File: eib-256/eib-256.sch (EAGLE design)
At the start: 36 parts

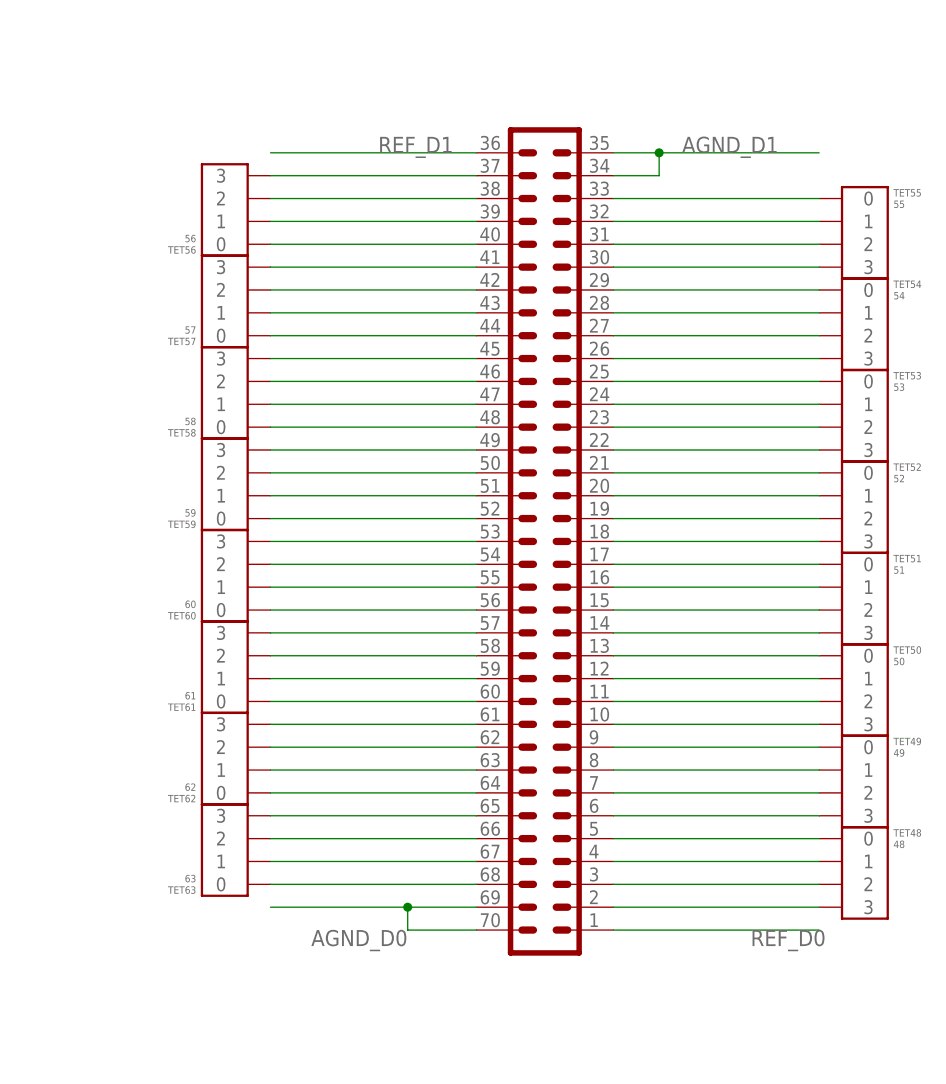
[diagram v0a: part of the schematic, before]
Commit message: More than half way through 256 channel eib layout.
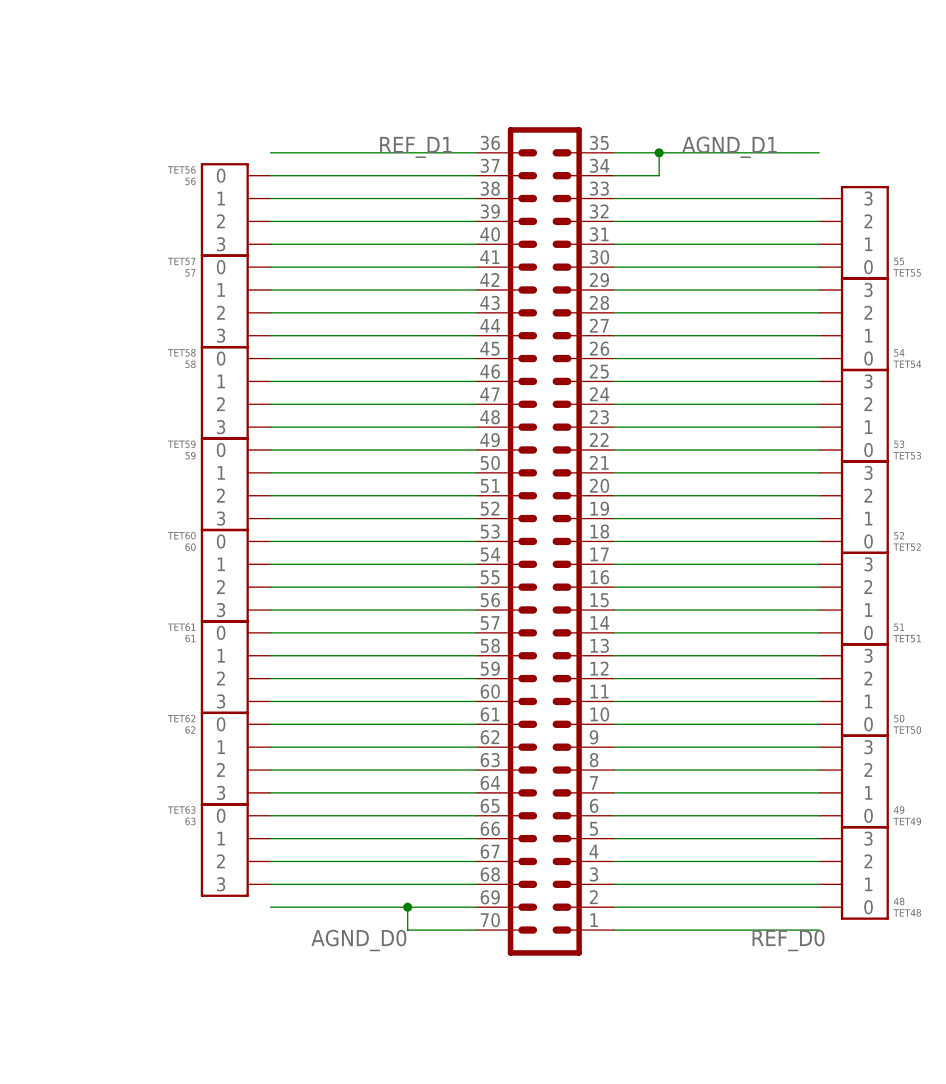
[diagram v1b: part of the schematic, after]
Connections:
- net N$1: now also D.2, TET48.0; no longer D.33, TET55.0
- net N$10: now also D.11, TET50.1; no longer D.24, TET53.1
- net N$11: now also D.12, TET50.2; no longer D.23, TET53.2
- net N$12: now also D.13, TET50.3; no longer D.22, TET53.3
- net N$13: now also D.14, TET51.0; no longer D.21, TET52.0
- net N$14: now also D.15, TET51.1; no longer D.20, TET52.1
- net N$15: now also D.16, TET51.2; no longer D.19, TET52.2
- net N$16: now also D.17, TET51.3; no longer D.18, TET52.3
- net N$17: now also D.18, TET52.0; no longer D.17, TET51.0
- net N$18: now also D.19, TET52.1; no longer D.16, TET51.1
- net N$19: now also D.20, TET52.2; no longer D.15, TET51.2
- net N$2: now also D.3, TET48.1; no longer D.32, TET55.1
- net N$20: now also D.21, TET52.3; no longer D.14, TET51.3
- net N$21: now also D.22, TET53.0; no longer D.13, TET50.0
- net N$22: now also D.23, TET53.1; no longer D.12, TET50.1
- net N$23: now also D.24, TET53.2; no longer D.11, TET50.2
- net N$24: now also D.25, TET53.3; no longer D.10, TET50.3
- net N$25: now also D.26, TET54.0; no longer D.9, TET49.0
- net N$26: now also D.27, TET54.1; no longer D.8, TET49.1
- net N$27: now also D.28, TET54.2; no longer D.7, TET49.2
- net N$28: now also D.29, TET54.3; no longer D.6, TET49.3
- net N$29: now also D.30, TET55.0; no longer D.5, TET48.0
- net N$3: now also D.4, TET48.2; no longer D.31, TET55.2
- net N$30: now also D.31, TET55.1; no longer D.4, TET48.1
- net N$31: now also D.32, TET55.2; no longer D.3, TET48.2
- net N$32: now also D.42, TET57.1; no longer D.38, TET56.2
- net N$33: now also D.43, TET57.2; no longer D.39, TET56.1
- net N$34: now also D.44, TET57.3; no longer D.40, TET56.0
- net N$35: now also D.45, TET58.0; no longer D.41, TET57.3
- net N$36: now also D.46, TET58.1; no longer D.42, TET57.2
- net N$37: now also D.47, TET58.2; no longer D.43, TET57.1
- net N$38: now also D.48, TET58.3; no longer D.44, TET57.0
- net N$39: now also D.49, TET59.0; no longer D.45, TET58.3
- net N$4: now also D.5, TET48.3; no longer D.30, TET55.3
- net N$40: now also D.50, TET59.1; no longer D.46, TET58.2
- net N$41: now also D.51, TET59.2; no longer D.47, TET58.1
- net N$42: now also D.52, TET59.3; no longer D.48, TET58.0
- net N$43: now also D.53, TET60.0; no longer D.49, TET59.3
- net N$44: now also D.54, TET60.1; no longer D.50, TET59.2
- net N$45: now also D.55, TET60.2; no longer D.51, TET59.1
- net N$46: now also D.56, TET60.3; no longer D.52, TET59.0
- net N$47: now also D.57, TET61.0; no longer D.53, TET60.3
- net N$48: now also D.58, TET61.1; no longer D.54, TET60.2
- net N$49: now also D.59, TET61.2; no longer D.55, TET60.1
- net N$5: now also D.6, TET49.0; no longer D.29, TET54.0
- net N$50: now also D.60, TET61.3; no longer D.56, TET60.0
- net N$51: now also D.61, TET62.0; no longer D.57, TET61.3
- net N$52: now also D.62, TET62.1; no longer D.58, TET61.2
- net N$53: now also D.63, TET62.2; no longer D.59, TET61.1
- net N$54: now also D.64, TET62.3; no longer D.60, TET61.0
- net N$55: now also D.65, TET63.0; no longer D.61, TET62.3
- net N$56: now also D.66, TET63.1; no longer D.62, TET62.2
- net N$57: now also D.67, TET63.2; no longer D.63, TET62.1
- net N$58: now also D.68, TET63.3; no longer D.64, TET62.0
- net N$59: now also D.41, TET57.0; no longer D.65, TET63.3
- net N$6: now also D.7, TET49.1; no longer D.28, TET54.1
- net N$60: now also D.40, TET56.3; no longer D.66, TET63.2
- net N$61: now also D.39, TET56.2; no longer D.67, TET63.1
- net N$62: now also D.38, TET56.1; no longer D.68, TET63.0
- net N$63: now also D.33, TET55.3; no longer D.2, TET48.3
- net N$64: now also TET56.0; no longer TET56.3
- net N$7: now also D.8, TET49.2; no longer D.27, TET54.2
- net N$8: now also D.9, TET49.3; no longer D.26, TET54.3
- net N$9: now also D.10, TET50.0; no longer D.25, TET53.0
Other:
- moved on the sheet: TET48, TET49, TET50, TET51, TET52, TET53, TET54, TET55, TET56, TET57, TET58, TET59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

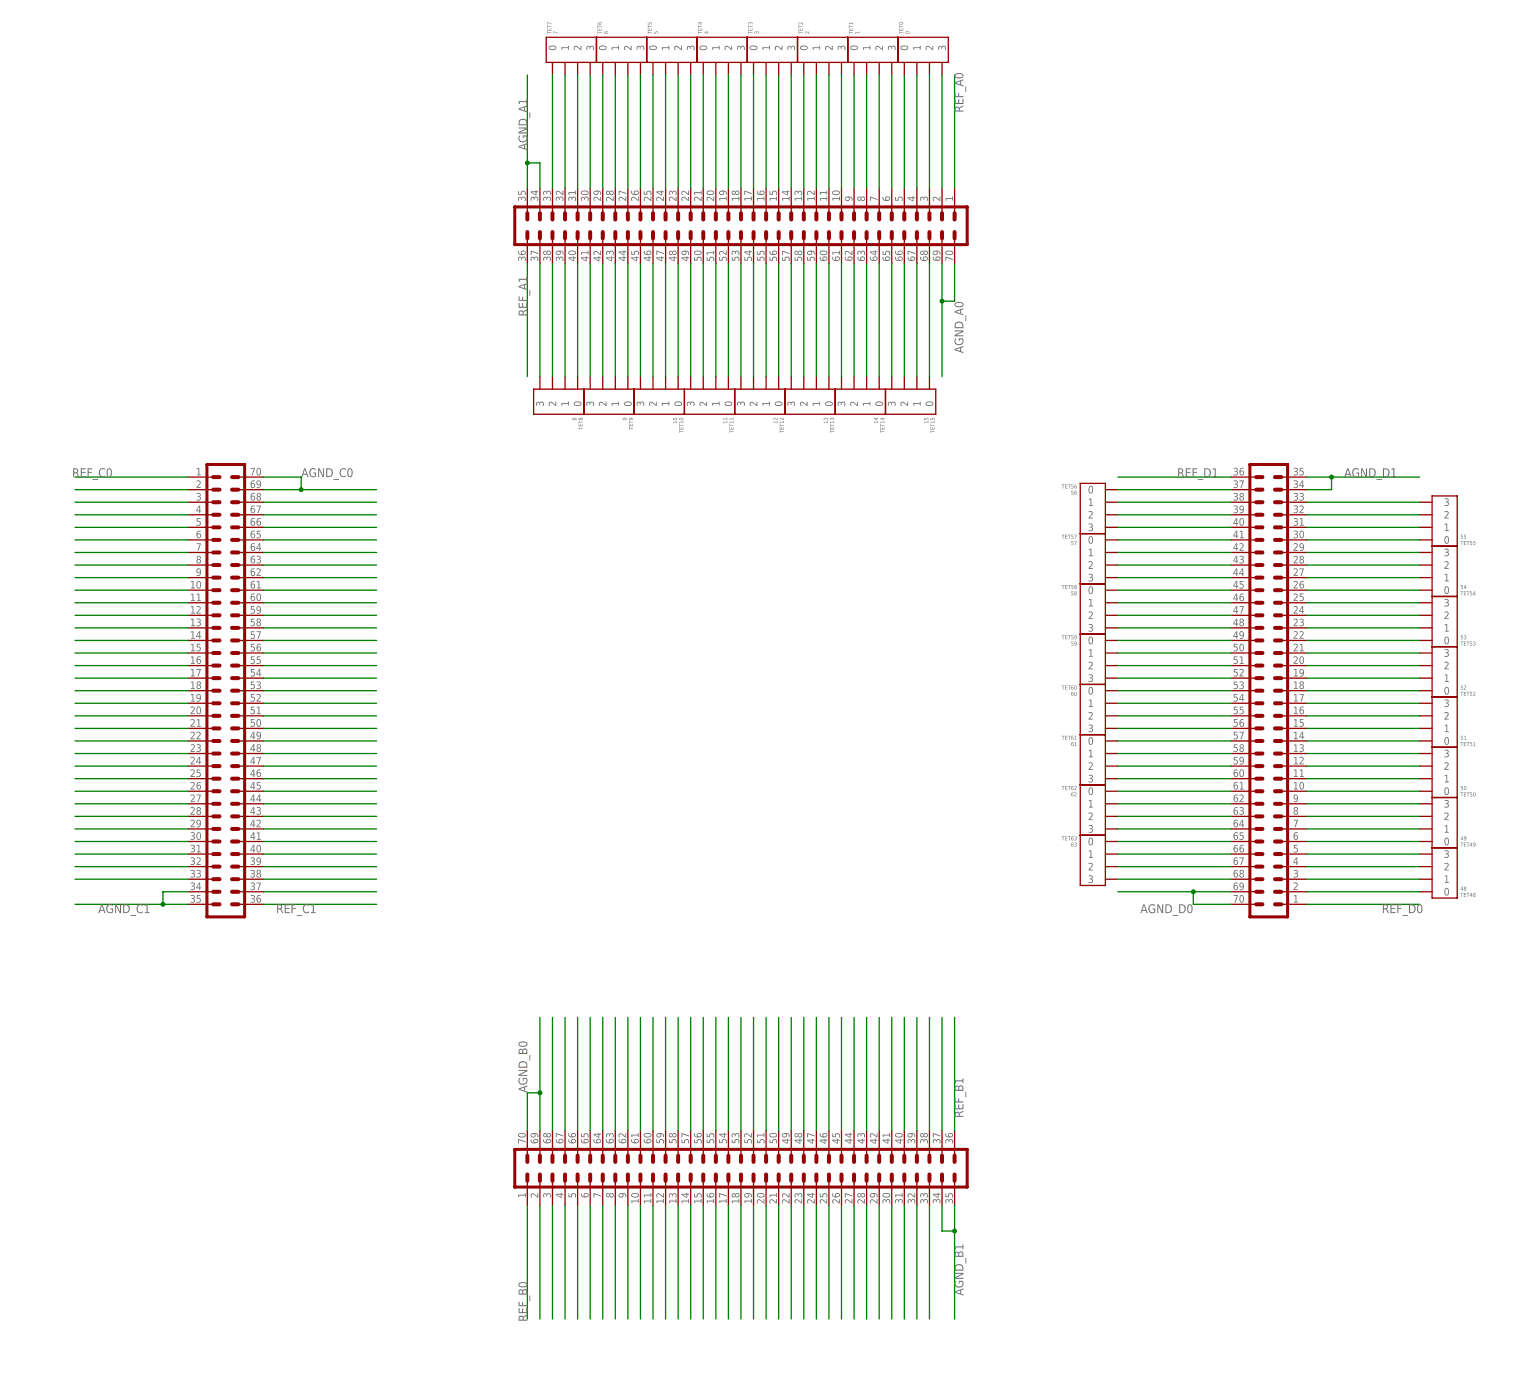
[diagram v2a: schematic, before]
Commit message: 256 eib tetrode layout complete. Needs ground and ref connections.
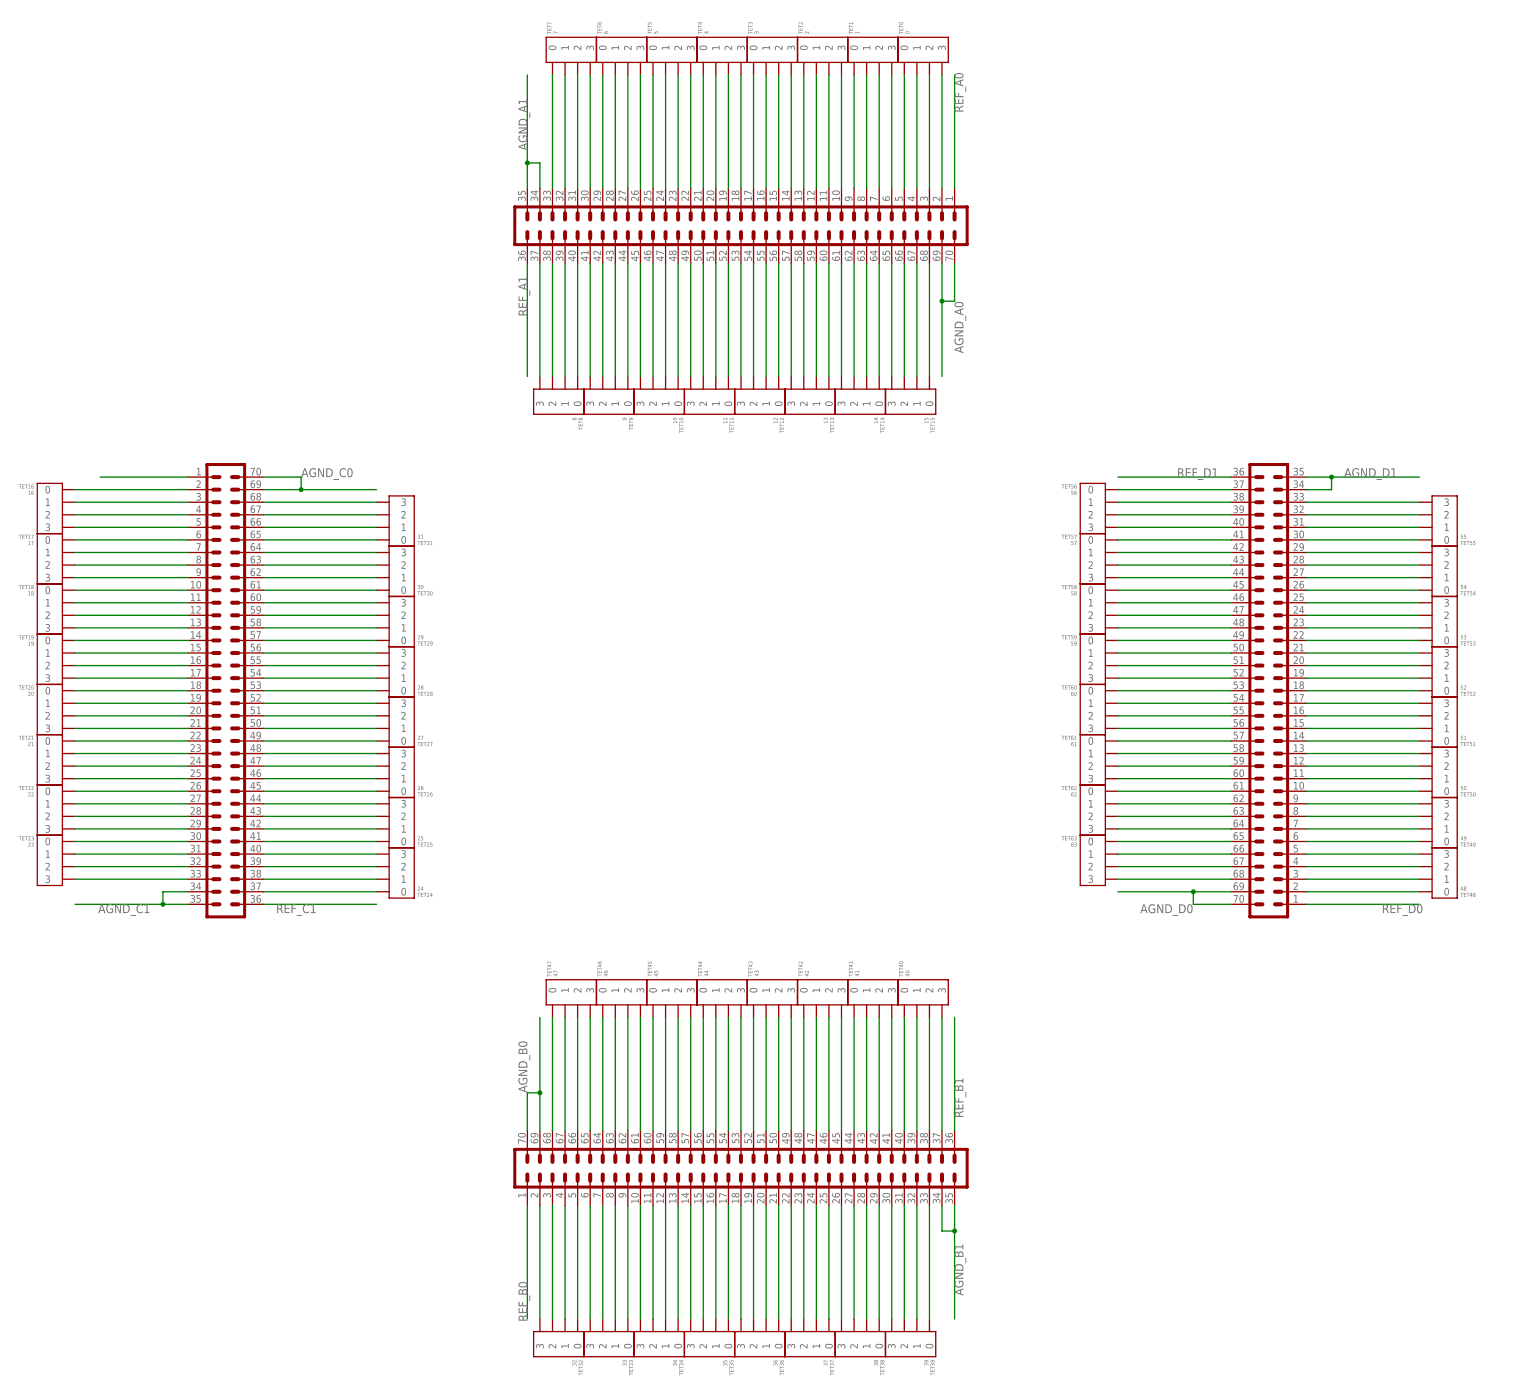
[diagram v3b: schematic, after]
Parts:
- added TET16: 16, jonnew:TETRODE_0.3ID_LINEAR
- added TET17: 17, jonnew:TETRODE_0.3ID_LINEAR
- added TET18: 18, jonnew:TETRODE_0.3ID_LINEAR
- added TET19: 19, jonnew:TETRODE_0.3ID_LINEAR
- added TET20: 20, jonnew:TETRODE_0.3ID_LINEAR
- added TET21: 21, jonnew:TETRODE_0.3ID_LINEAR
- added TET22: 22, jonnew:TETRODE_0.3ID_LINEAR
- added TET23: 23, jonnew:TETRODE_0.3ID_LINEAR
- added TET24: 24, jonnew:TETRODE_0.3ID_LINEAR
- added TET25: 25, jonnew:TETRODE_0.3ID_LINEAR
- added TET26: 26, jonnew:TETRODE_0.3ID_LINEAR
- added TET27: 27, jonnew:TETRODE_0.3ID_LINEAR
- added TET28: 28, jonnew:TETRODE_0.3ID_LINEAR
- added TET29: 29, jonnew:TETRODE_0.3ID_LINEAR
- added TET30: 30, jonnew:TETRODE_0.3ID_LINEAR
- added TET31: 31, jonnew:TETRODE_0.3ID_LINEAR
- added TET32: 32, jonnew:TETRODE_0.3ID_LINEAR
- added TET33: 33, jonnew:TETRODE_0.3ID_LINEAR
- added TET34: 34, jonnew:TETRODE_0.3ID_LINEAR
- added TET35: 35, jonnew:TETRODE_0.3ID_LINEAR
- added TET36: 36, jonnew:TETRODE_0.3ID_LINEAR
- added TET37: 37, jonnew:TETRODE_0.3ID_LINEAR
- added TET38: 38, jonnew:TETRODE_0.3ID_LINEAR
- added TET39: 39, jonnew:TETRODE_0.3ID_LINEAR
- added TET40: 40, jonnew:TETRODE_0.3ID_LINEAR
- added TET41: 41, jonnew:TETRODE_0.3ID_LINEAR
- added TET42: 42, jonnew:TETRODE_0.3ID_LINEAR
- added TET43: 43, jonnew:TETRODE_0.3ID_LINEAR
- added TET44: 44, jonnew:TETRODE_0.3ID_LINEAR
- added TET45: 45, jonnew:TETRODE_0.3ID_LINEAR
- added TET46: 46, jonnew:TETRODE_0.3ID_LINEAR
- added TET47: 47, jonnew:TETRODE_0.3ID_LINEAR
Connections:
- removed net N$100: B.42
- removed net N$101: B.43
- removed net N$102: B.44
- removed net N$103: B.45
- removed net N$104: B.46
- removed net N$105: B.47
- removed net N$106: B.48
- removed net N$107: B.49
- removed net N$108: B.50
- removed net N$109: B.51
- removed net N$110: B.52
- removed net N$111: B.53
- removed net N$112: B.54
- removed net N$113: B.55
- removed net N$114: B.56
- removed net N$115: B.57
- removed net N$116: B.58
- removed net N$117: B.59
- removed net N$118: B.60
- removed net N$119: B.61
- removed net N$120: B.62
- removed net N$121: B.63
- removed net N$122: B.64
- removed net N$123: B.65
- removed net N$124: B.66
- removed net N$125: B.67
- removed net N$126: B.68
- removed net N$127: B.2
- removed net N$128: B.37
- removed net N$129: C.33
- removed net N$130: C.32
- removed net N$131: C.31
- removed net N$132: C.30
- removed net N$133: C.29
- removed net N$134: C.28
- removed net N$135: C.27
- removed net N$136: C.26
- removed net N$137: C.25
- removed net N$138: C.24
- removed net N$139: C.23
- removed net N$140: C.22
- removed net N$141: C.21
- removed net N$142: C.20
- removed net N$143: C.19
- removed net N$144: C.18
- removed net N$145: C.17
- removed net N$146: C.16
- removed net N$147: C.15
- removed net N$148: C.14
- removed net N$149: C.13
- removed net N$150: C.12
- removed net N$151: C.11
- removed net N$152: C.10
- removed net N$153: C.9
- removed net N$154: C.8
- removed net N$155: C.7
- removed net N$156: C.6
- removed net N$157: C.5
- removed net N$158: C.4
- removed net N$159: C.3
- removed net N$160: C.38
- removed net N$161: C.39
- removed net N$162: C.40
- removed net N$163: C.41
- removed net N$164: C.42
- removed net N$165: C.43
- removed net N$166: C.44
- removed net N$167: C.45
- removed net N$168: C.46
- removed net N$169: C.47
- removed net N$170: C.48
- removed net N$171: C.49
- removed net N$172: C.50
- removed net N$173: C.51
- removed net N$174: C.52
- removed net N$175: C.53
- removed net N$176: C.54
- removed net N$177: C.55
- removed net N$178: C.56
- removed net N$179: C.57
- removed net N$180: C.58
- removed net N$181: C.59
- removed net N$182: C.60
- removed net N$183: C.61
- removed net N$184: C.62
- removed net N$185: C.63
- removed net N$186: C.64
- removed net N$187: C.65
- removed net N$188: C.66
- removed net N$189: C.67
- removed net N$190: C.68
- removed net N$191: C.2
- removed net N$192: C.37
- removed net N$97: B.39
- removed net N$98: B.40
- removed net N$99: B.41
- new net N$193: B.33, TET39.0
- new net N$194: B.32, TET39.1
- new net N$195: B.31, TET39.2
- new net N$196: B.30, TET39.3
- new net N$197: B.29, TET38.0
- new net N$198: B.28, TET38.1
- new net N$262: B.27, TET38.2
- new net N$263: B.26, TET38.3
- new net N$264: B.25, TET37.0
- new net N$265: B.24, TET37.1
- new net N$266: B.23, TET37.2
- new net N$267: B.22, TET37.3
- new net N$268: B.21, TET36.0
- new net N$269: B.20, TET36.1
- new net N$270: B.19, TET36.2
- new net N$271: B.18, TET36.3
- new net N$272: B.17, TET35.0
- new net N$273: B.16, TET35.1
- new net N$274: B.15, TET35.2
- new net N$275: B.14, TET35.3
- new net N$276: B.13, TET34.0
- new net N$277: B.12, TET34.1
- new net N$278: B.11, TET34.2
- new net N$279: B.10, TET34.3
- new net N$280: B.9, TET33.0
- new net N$281: B.8, TET33.1
- new net N$282: B.7, TET33.2
- new net N$283: B.6, TET33.3
- new net N$284: B.5, TET32.0
- new net N$285: B.4, TET32.1
- new net N$286: B.3, TET32.2
- new net N$287: B.38, TET40.2
- new net N$288: B.39, TET40.1
- new net N$289: B.40, TET40.0
- new net N$290: B.41, TET41.3
- new net N$291: B.42, TET41.2
- new net N$292: B.43, TET41.1
- new net N$293: B.44, TET41.0
- new net N$294: B.45, TET42.3
- new net N$295: B.46, TET42.2
- new net N$296: B.47, TET42.1
- new net N$297: B.48, TET42.0
- new net N$298: B.49, TET43.3
- new net N$299: B.50, TET43.2
- new net N$300: B.51, TET43.1
- new net N$301: B.52, TET43.0
- new net N$302: B.53, TET44.3
- new net N$303: B.54, TET44.2
- new net N$304: B.55, TET44.1
- new net N$305: B.56, TET44.0
- new net N$306: B.57, TET45.3
- new net N$307: B.58, TET45.2
- new net N$308: B.59, TET45.1
- new net N$309: B.60, TET45.0
- new net N$310: B.61, TET46.3
- new net N$311: B.62, TET46.2
- new net N$312: B.63, TET46.1
- new net N$313: B.64, TET46.0
- new net N$314: B.65, TET47.3
- new net N$315: B.66, TET47.2
- new net N$316: B.67, TET47.1
- new net N$317: B.68, TET47.0
- new net N$318: B.2, TET32.3
- new net N$319: B.37, TET40.3
- new net N$322: C.4, TET16.2
- new net N$323: C.5, TET16.3
- new net N$324: C.6, TET17.0
- new net N$326: C.7, TET17.1
- new net N$328: C.10, TET18.0
- new net N$330: C.11, TET18.1
- new net N$332: C.14, TET19.0
- new net N$334: C.15, TET19.1
- new net N$336: C.18, TET20.0
- new net N$338: C.19, TET20.1
- new net N$340: C.22, TET21.0
- new net N$341: C.23, TET21.1
- new net N$345: C.27, TET22.1
- new net N$347: C.26, TET22.0
- new net N$348: C.30, TET23.0
- new net N$350: C.31, TET23.1
- new net N$352: C.43, TET25.2
- new net N$354: C.48, TET26.3
- new net N$356: C.47, TET26.2
- new net N$358: C.52, TET27.3
- new net N$360: C.51, TET27.2
- new net N$362: C.56, TET28.3
- new net N$364: C.55, TET28.2
- new net N$366: C.60, TET29.3
- new net N$368: C.59, TET29.2
- new net N$370: C.61, TET30.0
- new net N$372: C.63, TET30.2
- new net N$374: C.68, TET31.3
- new net N$376: C.67, TET31.2
- new net N$379: C.44, TET25.3
- new net N$382: C.39, TET24.2
- new net N$383: C.40, TET24.3
- net N$65: now also C.3, TET16.1; no longer B.33
- net N$66: now also C.2, TET16.0; no longer B.32
- net N$67: now also C.32, TET23.2; no longer B.31
- net N$68: now also C.33, TET23.3; no longer B.30
- net N$69: now also C.28, TET22.2; no longer B.29
- net N$70: now also C.29, TET22.3; no longer B.28
- net N$71: now also C.24, TET21.2; no longer B.27
- net N$72: now also C.25, TET21.3; no longer B.26
- net N$73: now also C.20, TET20.2; no longer B.25
- net N$74: now also C.21, TET20.3; no longer B.24
- net N$75: now also C.16, TET19.2; no longer B.23
- net N$76: now also C.17, TET19.3; no longer B.22
- net N$77: now also C.12, TET18.2; no longer B.21
- net N$78: now also C.13, TET18.3; no longer B.20
- net N$79: now also C.8, TET17.2; no longer B.19
- net N$80: now also C.9, TET17.3; no longer B.18
- net N$81: now also C.66, TET31.1; no longer B.17
- net N$82: now also C.65, TET31.0; no longer B.16
- net N$83: now also C.62, TET30.1; no longer B.15
- net N$84: now also C.64, TET30.3; no longer B.14
- net N$85: now also C.58, TET29.1; no longer B.13
- net N$86: now also C.57, TET29.0; no longer B.12
- net N$87: now also C.54, TET28.1; no longer B.11
- net N$88: now also C.53, TET28.0; no longer B.10
- net N$89: now also C.49, TET27.0; no longer B.9
- net N$90: now also C.50, TET27.1; no longer B.8
- net N$91: now also C.46, TET26.1; no longer B.7
- net N$92: now also C.45, TET26.0; no longer B.6
- net N$93: now also C.42, TET25.1; no longer B.5
- net N$94: now also C.41, TET25.0; no longer B.4
- net N$95: now also C.38, TET24.1; no longer B.3
- net N$96: now also C.37, TET24.0; no longer B.38
